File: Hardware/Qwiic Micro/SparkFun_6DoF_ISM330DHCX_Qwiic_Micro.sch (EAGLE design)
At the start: 26 parts, among them J1 Qwiic Right Angle, U1 ISM330DHCX

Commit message: Moves test points to their designated areas, increases the size of most of the silk
* Moves to v10
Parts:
- removed J2: (no value), SparkFun-Connectors:CONN_02_1.5MM
- added J3, J4: (no value), SparkFun-Connectors:CONN_01_1MM
- added TP4: TEST-POINT3, SparkFun-Connectors:TEST-POINT3
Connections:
- net GND: now also J4.1, TP4.1; no longer J2.1
- net INT1: now also J3.1; no longer J2.2
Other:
- note added: "(Default)"
- note added: "v10"
- note removed: "v01"
- moved on the sheet: TP1, TP2, TP3

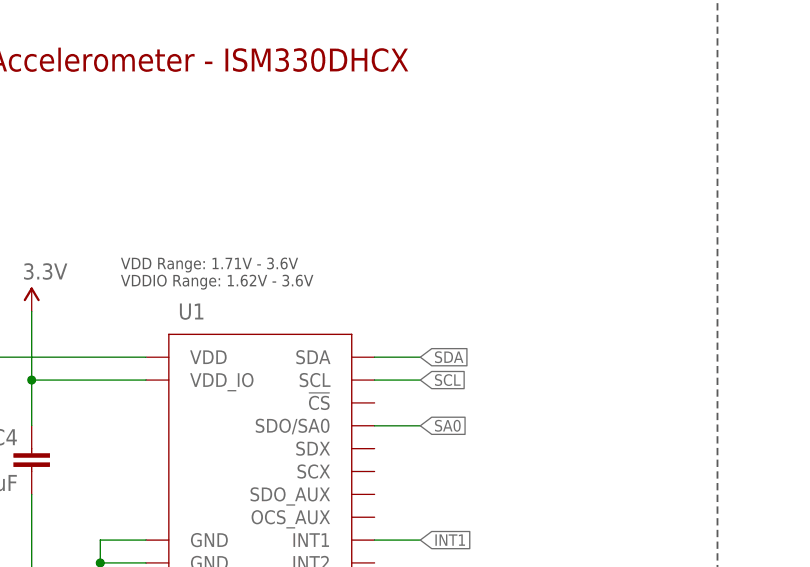
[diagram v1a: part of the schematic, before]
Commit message: adds 10k pullup on CS
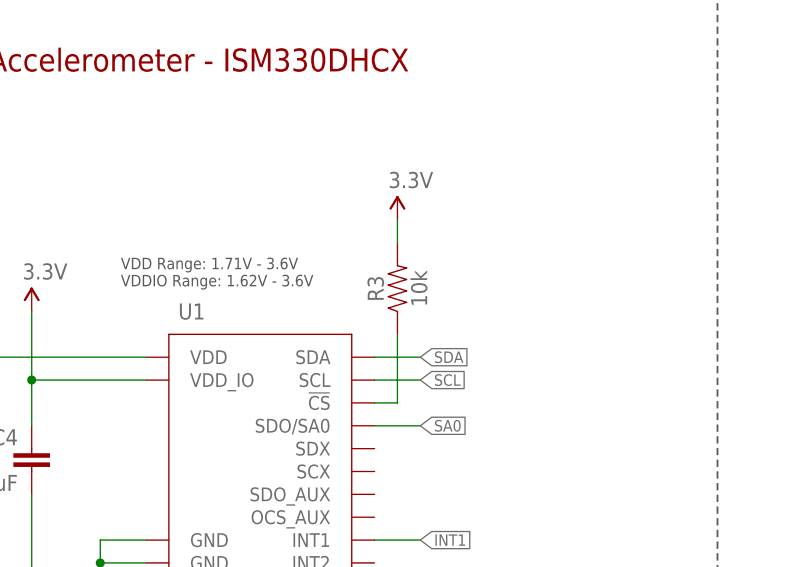
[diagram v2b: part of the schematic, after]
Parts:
- added R3: 10k, SparkFun-Resistors:10KOHM-0402T-1/16W-1%
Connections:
- new net N$4: R3.1, U1.!CS!
- net 3.3V: now also R3.2
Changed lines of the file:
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@@
 <part name="TP4" library="SparkFun-Connectors" deviceset="TEST-POINT" device="3" value="TEST-POINT3"/>
 <part name="GND1" library="SparkFun-PowerSymbols" deviceset="GND" device=""/>
+<part name="R3" library="SparkFun-Resistors" deviceset="10KOHM" device="-0402T-1/16W-1%" value="10k"/>
+<part name="SUPPLY7" library="SparkFun-PowerSymbols" deviceset="3.3V" device=""/>
 </parts>
 <sheets>
@@
 <attribute name="VALUE" x="96.52" y="86.36" size="1.778" layer="96" font="vector"/>
 </instance>
+<instance part="R3" gate="G$1" x="78.74" y="152.4" smashed="yes" rot="R90">
+<attribute name="NAME" x="77.216" y="152.4" size="1.778" layer="95" font="vector" rot="R90" align="bottom-center"/>
+<attribute name="VALUE" x="80.264" y="152.4" size="1.778" layer="96" font="vector" rot="R90" align="top-center"/>
+</instance>
+<instance part="SUPPLY7" gate="G$1" x="78.74" y="160.02" smashed="yes">
+<attribute name="VALUE" x="77.724" y="163.576" size="1.778" layer="96" font="vector"/>
+</instance>
 </instances>
 <busses>
@@
 <pinref part="SUPPLY6" gate="G$1" pin="3.3V"/>
 </segment>
+<segment>
+<pinref part="R3" gate="G$1" pin="2"/>
+<pinref part="SUPPLY7" gate="G$1" pin="3.3V"/>
+<wire x1="78.74" y1="160.02" x2="78.74" y2="157.48" width="0.1524" layer="91"/>
+</segment>
 </net>
 <net name="N$5" class="0">
@@
 </segment>
 </net>
+<net name="N$4" class="0">
+<segment>
+<pinref part="U1" gate="G$1" pin="!CS!"/>
+<wire x1="76.2" y1="139.7" x2="78.74" y2="139.7" width="0.1524" layer="91"/>
+<wire x1="78.74" y1="139.7" x2="78.74" y2="147.32" width="0.1524" layer="91"/>
+<pinref part="R3" gate="G$1" pin="1"/>
+</segment>
+</net>

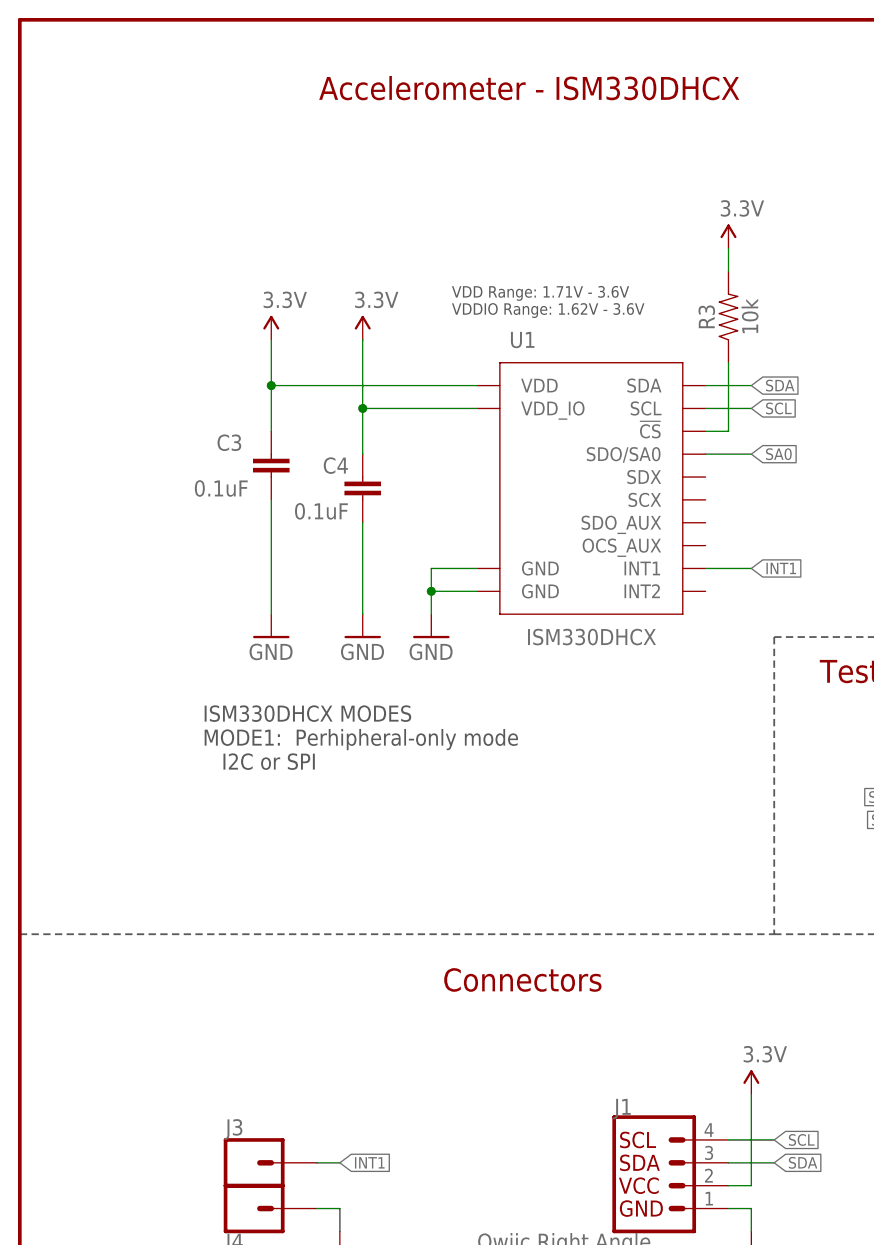
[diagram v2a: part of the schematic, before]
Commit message: Adds some text about i2c address and PTH connectors
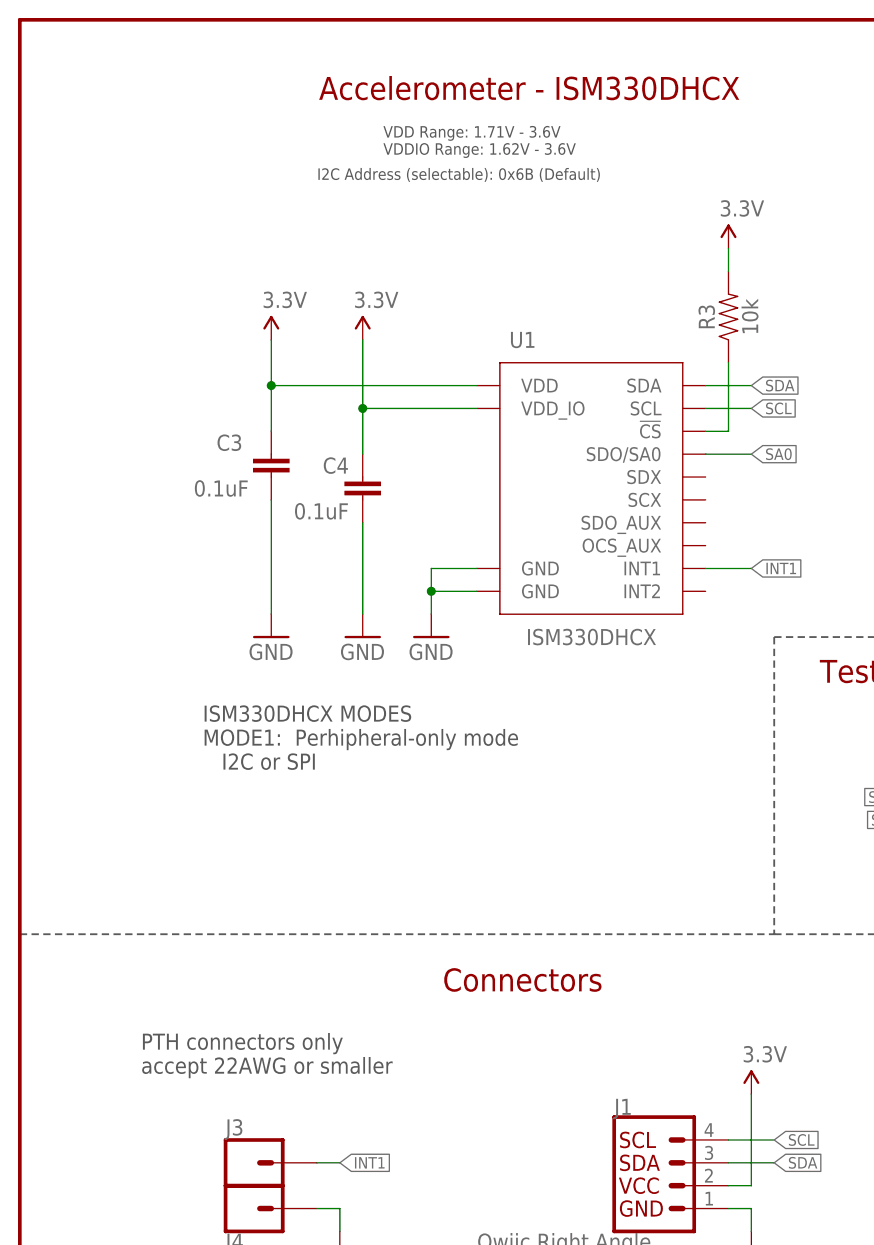
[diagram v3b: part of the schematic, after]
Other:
- note added: "I2C Address (selectable): 0x6B (Default)"
- note added: "PTH connectors only accept 22AWG or smaller"
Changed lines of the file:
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@@
 <wire x1="114.3" y1="83.82" x2="248.92" y2="83.82" width="0.2032" layer="97" style="longdash"/>
 <wire x1="114.3" y1="185.42" x2="114.3" y2="116.84" width="0.2032" layer="97" style="longdash"/>
-<text x="48.006" y="152.654" size="1.27" layer="97" font="vector">VDD Range: 1.71V - 3.6V
+<text x="40.386" y="170.434" size="1.27" layer="97" font="vector">VDD Range: 1.71V - 3.6V
 VDDIO Range: 1.62V - 3.6V</text>
 <text x="238.76" y="7.62" size="2.54" layer="94" font="vector">v10</text>
@@
 <wire x1="83.82" y1="116.84" x2="83.82" y2="83.82" width="0.2032" layer="97" style="longdash"/>
 <wire x1="83.82" y1="83.82" x2="114.3" y2="83.82" width="0.2032" layer="97" style="longdash"/>
+<text x="33.02" y="167.64" size="1.27" layer="97" font="vector">I2C Address (selectable): 0x6B (Default)</text>
+<text x="13.462" y="68.326" size="1.778" layer="97" font="vector">PTH connectors only
+accept 22AWG or smaller</text>
 </plain>
 <instances>

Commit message: Renames production files to include version number, updates 0402 RED LED with one that has PROD_ID
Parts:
- D1: device ISM330DHCX:LED_0402 -> SparkFun-LED:LED-RED_0402
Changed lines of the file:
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@@
 <part name="FD1" library="SparkFun-Aesthetics" deviceset="FIDUCIAL" device="UFIDUCIAL"/>
 <part name="FD2" library="SparkFun-Aesthetics" deviceset="FIDUCIAL" device="UFIDUCIAL"/>
-<part name="D1" library="ISM330DHCX" deviceset="LED_0402" device="" value="RED"/>
+<part name="D1" library="SparkFun-LED" deviceset="LED-RED" device="_0402" value="RED"/>
 <part name="R4" library="SparkFun-Resistors" deviceset="1KOHM" device="-0402T-1/16W-1%" value="1k"/>
 <part name="LED" library="SparkFun-Jumpers" deviceset="JUMPER-SMT_2_NC_TRACE" device="_SILK" package3d_urn="urn:adsk.eagle:package:39281/1"/>
